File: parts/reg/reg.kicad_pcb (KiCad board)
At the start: 2 copper layers, 71.6 x 106.7 mm, 53 parts, among them J1 Conn_02x02_Odd_Even, J2 Conn_02x04_Odd_Even, J3 Conn_02x04_Odd_Even, J4 Conn_01x02, J5 Conn_02x04_Odd_Even, K1 HK19F, K10 HK19F, K11 HK19F, K12 HK19F, K2 HK19F, K3 HK19F, K4 HK19F, K5 HK19F, K6 HK19F, K7 HK19F, K8 HK19F, K9 HK19F

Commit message: Update to new Kicad, finish reg.
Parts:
- added J6: Conn_02x04_Odd_Even, Pin_Headers:Pin_Header_Straight_2x04_Pitch2.54mm, F.Cu at (207.5, 39.6)
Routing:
- net Net-(D8-Pad1): track 22.1 -> 131.5 mm, vias 0 -> 2
- net Net-(D7-Pad1): track 28.7 -> 129.1 mm, vias 0 -> 2
- net Net-(D6-Pad1): track 22.3 -> 111.4 mm, vias 0 -> 2
- net Net-(D4-Pad1): track 23.3 -> 94.1 mm, vias 0 -> 1
- net Net-(D5-Pad1): track 28.5 -> 91.5 mm, vias 0 -> 2
- net Net-(D3-Pad1): track 28.1 -> 75.0 mm
- net Net-(D2-Pad1): track 24.9 -> 62.2 mm, vias 0 -> 1
- net Net-(D1-Pad1): track 27.5 -> 56.3 mm
- net GND: track 7.84 -> 10.7 mm, vias 0 -> 15
- net Net-(J3-Pad1): track 70.0 -> 68.6 mm
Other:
- board size 71.6 x 106.7 mm -> 72.6 x 106.7 mm
- board text added: "+"
- board text added: "1"
- board text added: "CLK/EN"
- board text added: "GND"
- board text added: "IN"
- board text added: "OUT"
- board text added: "OVER RIDE"
- board text added: "PWR"
- board text added: "~OUT"

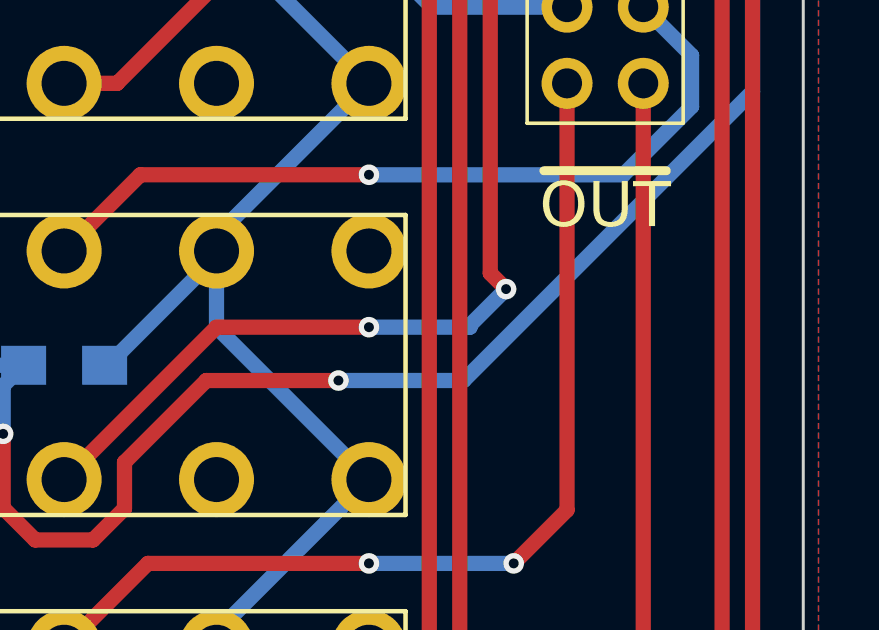
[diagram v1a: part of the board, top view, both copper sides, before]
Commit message: reg: Route missing GND connection.
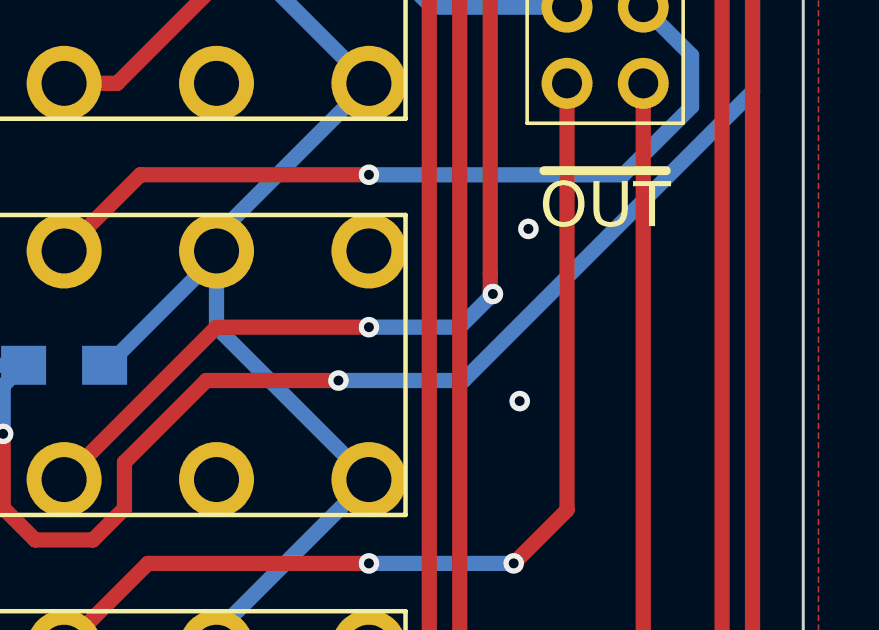
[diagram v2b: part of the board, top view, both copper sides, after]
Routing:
- net Net-(J2-Pad6): track 47.0 -> 46.4 mm
- net GND: vias 15 -> 17
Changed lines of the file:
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@@
-(kicad_pcb (version 20171130) (host pcbnew 5.0.1)
+(kicad_pcb (version 20171130) (host pcbnew 5.1.5)
   (general
     (thickness 1.6)
     (drawings 20)
-    (tracks 489)
+    (tracks 491)
     (zones 0)
     (modules 54)
@@
     (zone_45_only yes)
     (trace_min 0.1524)
-    (segment_width 0.2)
-    (edge_width 0.1)
     (via_size 0.6858)
     (via_drill 0.3302)
@@
     (uvia_min_size 0)
     (uvia_min_drill 0)
+    (edge_width 0.1)
+    (segment_width 0.2)
     (pcb_text_width 0.3)
     (pcb_text_size 1.5 1.5)
@@
   (via (at 200.406 77.978) (size 0.6858) (drill 0.3302) (layers F.Cu B.Cu) (net 14))
   (via (at 192.278 66.04) (size 0.6858) (drill 0.3302) (layers F.Cu B.Cu) (net 14))
+  (via (at 206.23 99.34) (size 0.6858) (drill 0.3302) (layers F.Cu B.Cu) (net 14))
+  (via (at 205.94 105.08) (size 0.6858) (drill 0.3302) (layers F.Cu B.Cu) (net 14))
   (segment (start 160.528 47.244) (end 170.18 47.244) (width 0.508) (layer F.Cu) (net 15))
   (segment (start 170.18 47.244) (end 173.228 44.196) (width 0.508) (layer F.Cu) (net 15))
@@
   (segment (start 207.518 78.74) (end 207.518 78.894238) (width 0.508) (layer F.Cu) (net 26))
   (segment (start 207.518 78.74) (end 207.518 78.894238) (width 0.508) (layer B.Cu) (net 26))
-  (segment (start 205.486 101.346) (end 204.958021 100.818021) (width 0.508) (layer F.Cu) (net 27))
   (segment (start 204.958021 100.818021) (end 204.958021 84.601979) (width 0.508) (layer F.Cu) (net 27))
-  (segment (start 204.284911 102.616) (end 204.284911 102.547089) (width 0.508) (layer B.Cu) (net 27))
-  (segment (start 204.284911 102.547089) (end 205.486 101.346) (width 0.508) (layer B.Cu) (net 27))
-  (via (at 205.486 101.346) (size 0.6858) (drill 0.3302) (layers F.Cu B.Cu) (net 27))
   (segment (start 200.914 102.616) (end 195.834 102.616) (width 0.508) (layer F.Cu) (net 27))
   (segment (start 195.834 102.616) (end 190.754 107.696) (width 0.508) (layer F.Cu) (net 27))
-  (segment (start 204.284911 102.616) (end 200.914 102.616) (width 0.508) (layer B.Cu) (net 27))
   (via (at 200.914 102.616) (size 0.6858) (drill 0.3302) (layers F.Cu B.Cu) (net 27))
   (segment (start 210.068925 83.908011) (end 205.651989 83.908011) (width 0.508) (layer F.Cu) (net 27))
@@
   (segment (start 211.670001 79.14992) (end 211.670001 82.306935) (width 0.508) (layer F.Cu) (net 27))
   (segment (start 211.670001 82.306935) (end 210.068925 83.908011) (width 0.508) (layer F.Cu) (net 27))
+  (via (at 205.046911 101.51) (size 0.6858) (drill 0.3302) (layers F.Cu B.Cu) (net 27))
+  (segment (start 204.958021 100.818021) (end 204.958021 101.42111) (width 0.508) (layer F.Cu) (net 27))
+  (segment (start 204.958021 101.42111) (end 205.046911 101.51) (width 0.508) (layer F.Cu) (net 27))
+  (segment (start 203.940911 102.616) (end 200.914 102.616) (width 0.508) (layer B.Cu) (net 27))
+  (segment (start 205.046911 101.51) (end 203.940911 102.616) (width 0.508) (layer B.Cu) (net 27))
   (segment (start 207.518 81.28) (end 205.328617 81.28) (width 0.508) (layer F.Cu) (net 28))
   (segment (start 205.328617 81.28) (end 202.926001 83.682616) (width 0.508) (layer F.Cu) (net 28))

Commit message: Git-ignore (old) parts directory, commit final changes there.
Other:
- net class Default removed
- net class Minimal removed
- board text added: "~{OUT}"
- board text removed: "~OUT"
